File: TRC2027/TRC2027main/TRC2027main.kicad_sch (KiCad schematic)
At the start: 55 parts, among them J1 Power_conn(XT90), J10 Memory, J11 BNO055, J12 Temperature, pressure, and al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, J13 Conn_01x03_Pin, J14 Conn_01x04_Pin, J15 Conn_01x04_Pin, J16 Conn_01x04_Pin, J17 Conn_01x04_Pin, J18 Conn_01x04_Pin, J19 Conn_01x12_Pin, J2 電圧計_測定, J20 Conn_01x10_Pin, J3 電圧計_電源, J4 XH_Moter_Output, J5 XH_Moter_Output, J6 Conn_01x07_Pin, J7 GPS, J8 Conn_01x08_Pin, J9 Conn_01x08_Pin, SW1 SW_SPST, U1 DCDC, U2 DRV8262DDWR, U3 DRV8262DDWR

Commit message: change DataSheet
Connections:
- no-connect marks 43 -> 44
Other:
- moved on the sheet: A1

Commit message: add TRC2027main/SW_LED
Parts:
- removed D3: LED_RGBA, symbol Device:LED_RGBA
- added IC1: MCP23017-E_SP, KiCad_MCP23017:DIP794W56P254L3486H508Q28N, symbol MCP23017-E_SP:MCP23017-E_SP
- added J21: Conn_01x04_Pin, Connector_JST:JST_XH_B4B-XH-A_1x04_P2.50mm_Vertical, symbol Connector:Conn_01x04_Pin
- added J22, J23: XH_Moter_Output, Connector_JST:JST_XH_B2B-XH-A_1x02_P2.50mm_Vertical, symbol Connector:Conn_01x02_Pin
- added J24, J25: Conn_01x04_Pin, LED_THT:LED_D5.0mm-4_RGB, symbol Connector:Conn_01x04_Pin
- added R10: 75, Resistor_THT:R_Axial_DIN0207_L6.3mm_D2.5mm_P10.16mm_Horizontal, symbol Device:R
- added R11: 10k, Resistor_THT:R_Axial_DIN0207_L6.3mm_D2.5mm_P10.16mm_Horizontal, symbol Device:R
- added R7, R8: 10, Resistor_THT:R_Axial_DIN0207_L6.3mm_D2.5mm_P10.16mm_Horizontal, symbol Device:R
- added R9: 330, Resistor_THT:R_Axial_DIN0207_L6.3mm_D2.5mm_P10.16mm_Horizontal, symbol Device:R
- added S1: ST12-303FCG, KiCad_ST12:ST12303FCG, symbol ST12-303FCG:ST12-303FCG
- added U4, U5: DRV8262DDWR, DRV8262DDWRModule:DRV8262DDWRModule, symbol DRV8262DDWRModule:DRV8262DDWRModule
- C3: footprint (none) -> Capacitor_THT:CP_Radial_D5.0mm_P2.00mm
- C6, C8: footprint (none) -> Capacitor_SMD:C_0603_1608Metric
- C7: footprint (none) -> Capacitor_THT:CP_Radial_D8.0mm_P3.50mm
- D1, D2: footprint (none) -> LED_THT:LED_D5.0mm
- D10, D11, D12, D13, D5, D6, D7, D9: footprint UCLAMP3381PTFT -> KiCad_UCLAMP3381:UCLAMP3381PTFT
- F2: footprint 3557-15:FUSE_3557-15 -> 3557-15_fuse:FUSE_3557-15
- J1: footprint (none) -> Connector_AMASS:AMASS_XT90PW-M_1x02_P10.90mm_Horizontal
- J13: footprint (none) -> Connector_PinHeader_2.54mm:PinHeader_1x03_P2.54mm_Vertical
- J14, J15, J17, J18: footprint (none) -> Connector_JST:JST_XH_B4B-XH-A_1x04_P2.50mm_Vertical
- J16: footprint (none) -> Connector_PinHeader_2.54mm:PinHeader_1x04_P2.54mm_Vertical
- J19: footprint (none) -> Connector_PinHeader_2.54mm:PinHeader_1x12_P2.54mm_Vertical
- J2, J3, J4, J5: footprint (none) -> Connector_JST:JST_XH_B2B-XH-A_1x02_P2.50mm_Vertical
- J20: footprint (none) -> Connector_PinHeader_2.54mm:PinHeader_1x10_P2.54mm_Vertical
- J6: footprint (none) -> Connector_PinHeader_2.54mm:PinHeader_1x07_P2.54mm_Vertical
- MD1: footprint OKL-T_6-W12N-C:MURATA_OKL-T-6-W12N-C_0 -> OKL_T_6_W12N_C:MURATA_OKL-T-6-W12N-C_0
- R1, R2, R3: footprint (none) -> Resistor_THT:R_Axial_DIN0207_L6.3mm_D2.5mm_P10.16mm_Horizontal
- R4: value 330Ω -> 330; footprint (none) -> Resistor_THT:R_Axial_DIN0207_L6.3mm_D2.5mm_P10.16mm_Horizontal
- R5, R6: value 47Ω -> 10; footprint (none) -> Resistor_THT:R_Axial_DIN0207_L6.3mm_D2.5mm_P10.16mm_Horizontal
- U2, U3: footprint (none) -> DRV8262DDWRModule:DRV8262DDWRModule
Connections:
- net +24V: now also U4.3 (VM), U5.3 (VM)
- net +3.3V: now also IC1.18 (~{RESET}), IC1.9 (VDD), R10.1, S1.1, U4.9 (VCC), U5.9 (VCC)
- net +5V: now also J21.2 (Pin_2)
- net AUX: now also IC1.5 (GPB4); no longer A1.16 (GPIO12)
- net AnFAULT: now also IC1.1 (GPB0); no longer A1.17 (GPIO13)
- net BnFAULT: now also IC1.2 (GPB1); no longer A1.19 (GPIO14)
- net GND: now also IC1.10 (VSS), IC1.15 (A0), IC1.16 (A1), IC1.17 (A2), IC1.27 (GPA6), J21.1 (Pin_1), J24.2 (Pin_2), J25.2 (Pin_2), R11.1, S1.MH2, U4.4 (GND), U4.8 (GND), U5.4 (GND), U5.8 (GND)
- net PWRKEY: now also IC1.7 (GPB6); no longer A1.32 (GPIO27_ADC1)
- net RESET: now also IC1.8 (GPB7); no longer A1.31 (GPIO26_ADC0)
- net RST1: now also IC1.6 (GPB5); no longer A1.20 (GPIO15)
- net SCL: now also IC1.12 (SCL)
- net SDA: now also IC1.13 (SDA)
- net LED1: now reaches R4.2
- net LED1: now also IC1.21 (GPA0)
- net at R5.1: now also J24.3 (Pin_3)
- net LED3: now reaches R6.2
- net LED3: now also IC1.23 (GPA2)
- net GP20: no longer names the net of R4.1
- net GP20: now also J24.1 (Pin_1); no longer A1.26 (GPIO20)
- net GP21 renamed DIN2
- net DIN2: now also U5.6 (IN2); no longer R5.2
- net GP22: no longer names the net of R6.1
- net GP22: now also J24.4 (Pin_4); no longer A1.29 (GPIO22)
- net M0: no longer names the net of J6.1 (Pin_1)
- net M0: no longer A1.14 (GPIO10)
- net M1: no longer names the net of J6.2 (Pin_2)
- net M1: no longer A1.15 (GPIO11)
- new net: R11.2, S1.3
- new net: R10.2, S1.MH1
- new net: J25.1 (Pin_1), R9.1
- new net: J25.4 (Pin_4), R7.1
- new net: J25.3 (Pin_3), R8.1
- new net CIN1: A1.14 (GPIO10), U4.7 (IN1)
- new net CIN2: A1.15 (GPIO11), U4.6 (IN2)
- new net COUT1: J23.1 (Pin_1), U4.1 (OUT1)
- new net COUT2: J23.2 (Pin_2), U4.2 (OUT2)
- new net CnFAULT: IC1.3 (GPB2), U4.5 (nFAULT)
- new net DIN1: A1.26 (GPIO20), U5.7 (IN1)
- new net DOUT1: J22.1 (Pin_1), U5.1 (OUT1)
- new net DOUT2: J22.2 (Pin_2), U5.2 (OUT2)
- new net DnFAULT: IC1.4 (GPB3), U5.5 (nFAULT)
- new net LED2: IC1.22 (GPA1), R5.2
- new net LED4: IC1.24 (GPA3), R9.2
- new net LED5: IC1.25 (GPA4), R8.2
- new net LED6: IC1.26 (GPA5), R7.2
- no-connect marks 44 -> 53
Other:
- moved on the sheet: A1, C3, D12, D13, D5, D6, J16, J4, J5

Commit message: new file:   TRC2027/R_Sokutei/R_Sokutei-backups/R_Sokutei-2026-04-18_181141.zip
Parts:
- added C10, C11, C9: 100u, Capacitor_THT:CP_Radial_D8.0mm_P3.50mm, symbol Device:C_Polarized
- added D3, D4: UCLAMP3381P.TFT, KiCad_UCLAMP3381:UCLAMP3381PTFT, symbol UCLAMP3381P_TFT:UCLAMP3381P.TFT
- added J26, J27, J28: Conn_01x03_Pin, Connector_JST:JST_XH_B3B-XH-A_1x03_P2.50mm_Vertical, symbol Connector:Conn_01x03_Pin
- J24, J25: footprint LED_THT:LED_D5.0mm-4_RGB -> Connector_JST:JST_XH_B4B-XH-A_1x04_P2.50mm_Vertical
- MD1: footprint OKL_T_6_W12N_C:MURATA_OKL-T-6-W12N-C_0 -> OKL_T_6_W12N_C:OKL-T&slash_6-W12N-C-Kai
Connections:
- net +5V: now also C10.1, C11.1, C9.1, J26.2 (Pin_2), J27.2 (Pin_2), J28.2 (Pin_2)
- net GND: now also C10.2, C11.2, C9.2, D3.2, D4.2, J26.1 (Pin_1), J27.1 (Pin_1), J28.1 (Pin_1); no longer IC1.27 (GPA6)
- net RX2: now also J21.4 (Pin_4), D3.1
- net TX2: now also J21.3 (Pin_3), D4.1
- net LEDSW: now reaches R11.2, S1.3
- net LEDSW: now also IC1.27 (GPA6)
- net PWM: now reaches A1.16 (GPIO12)
- net PWM: now also J26.3 (Pin_3)
- net PWM2: now reaches A1.17 (GPIO13)
- net PWM2: now also J27.3 (Pin_3)
- net PWM3: now reaches A1.19 (GPIO14)
- net PWM3: now also J28.3 (Pin_3)
- no-connect marks 53 -> 51
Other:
- moved on the sheet: R11

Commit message: add
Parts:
- removed A1: RaspberryPi_Pico, Module:RaspberryPi_Pico_Common_Unspecified, symbol MCU_Module:RaspberryPi_Pico
- removed C10: 100u, Capacitor_THT:CP_Radial_D8.0mm_P3.50mm, symbol Device:C_Polarized
- removed C3: 47u, Capacitor_THT:CP_Radial_D5.0mm_P2.00mm, symbol Device:C_Polarized
- removed D10, D11, D12, D13, D3, D4, D5, D6, D7, D9: UCLAMP3381P.TFT, KiCad_UCLAMP3381:UCLAMP3381PTFT, symbol UCLAMP3381P_TFT:UCLAMP3381P.TFT
- removed IC1: MCP23017-E_SP, KiCad_MCP23017:DIP794W56P254L3486H508Q28N, symbol MCP23017-E_SP:MCP23017-E_SP
- removed J10: Memory, Connector_PinSocket_2.54mm:PinSocket_1x07_P2.54mm_Vertical, symbol Connector:Conn_01x07_Pin
- removed J11: BNO055, Connector_PinSocket_2.54mm:PinSocket_1x04_P2.54mm_Vertical, symbol Connector:Conn_01x04_Pin
- removed J12: Temperature, pressure, and altitude sensor, Connector_PinSocket_2.54mm:PinSocket_1x07_P2.54mm_Vertical, symbol Connector:Conn_01x07_Pin
- removed J13: Conn_01x03_Pin, Connector_PinHeader_2.54mm:PinHeader_1x03_P2.54mm_Vertical, symbol Connector:Conn_01x03_Pin
- removed J14, J15, J17, J18, J21, J24, J25: Conn_01x04_Pin, Connector_JST:JST_XH_B4B-XH-A_1x04_P2.50mm_Vertical, symbol Connector:Conn_01x04_Pin
- removed J16: Conn_01x04_Pin, Connector_PinHeader_2.54mm:PinHeader_1x04_P2.54mm_Vertical, symbol Connector:Conn_01x04_Pin
- removed J19: Conn_01x12_Pin, Connector_PinHeader_2.54mm:PinHeader_1x12_P2.54mm_Vertical, symbol Connector:Conn_01x12_Pin
- removed J20: Conn_01x10_Pin, Connector_PinHeader_2.54mm:PinHeader_1x10_P2.54mm_Vertical, symbol Connector:Conn_01x10_Pin
- removed J6: Conn_01x07_Pin, Connector_PinHeader_2.54mm:PinHeader_1x07_P2.54mm_Vertical, symbol Connector:Conn_01x07_Pin
- removed J7: GPS, Connector_PinSocket_2.54mm:PinSocket_1x04_P2.54mm_Vertical, symbol Connector:Conn_01x04_Pin
- removed J8, J9: Conn_01x08_Pin, Connector_PinHeader_2.54mm:PinHeader_1x08_P2.54mm_Vertical, symbol Connector:Conn_01x08_Pin
- removed R10: 75, Resistor_THT:R_Axial_DIN0207_L6.3mm_D2.5mm_P10.16mm_Horizontal, symbol Device:R
- removed R11: 10k, Resistor_THT:R_Axial_DIN0207_L6.3mm_D2.5mm_P10.16mm_Horizontal, symbol Device:R
- removed R4, R9: 330, Resistor_THT:R_Axial_DIN0207_L6.3mm_D2.5mm_P10.16mm_Horizontal, symbol Device:R
- removed R5, R6, R7, R8: 10, Resistor_THT:R_Axial_DIN0207_L6.3mm_D2.5mm_P10.16mm_Horizontal, symbol Device:R
- removed S1: ST12-303FCG, KiCad_ST12:ST12303FCG, symbol ST12-303FCG:ST12-303FCG
- added J30: Conn_01x20_Pin, Connector_JST:JST_XH_B20B-XH-A_1x20_P2.50mm_Vertical, symbol Connector:Conn_01x20_Pin
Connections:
- net +3.3V: now also J30.4 (Pin_4)
- net +5V: now also J30.5 (Pin_5)
- net AIN1: now also J30.20 (Pin_20)
- net AIN2: now also J30.19 (Pin_19)
- net AnFAULT: now also J30.9 (Pin_9)
- net BIN1: now also J30.18 (Pin_18)
- net BIN2: now also J30.17 (Pin_17)
- net BnFAULT: now also J30.8 (Pin_8)
- net CIN1: now also J30.16 (Pin_16)
- net CIN2: now also J30.15 (Pin_15)
- net CnFAULT: now also J30.7 (Pin_7)
- net DIN1: now also J30.14 (Pin_14)
- net DIN2: now also J30.13 (Pin_13)
- net DnFAULT: now also J30.6 (Pin_6)
- net GND: now also J30.3 (Pin_3)
- net PWM: now also J30.12 (Pin_12)
- net PWM2: now also J30.11 (Pin_11)
- net PWM3: now also J30.10 (Pin_10)
- no-connect marks 51 -> 11
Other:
- moved on the sheet: C11, C9, J26, J27, J28

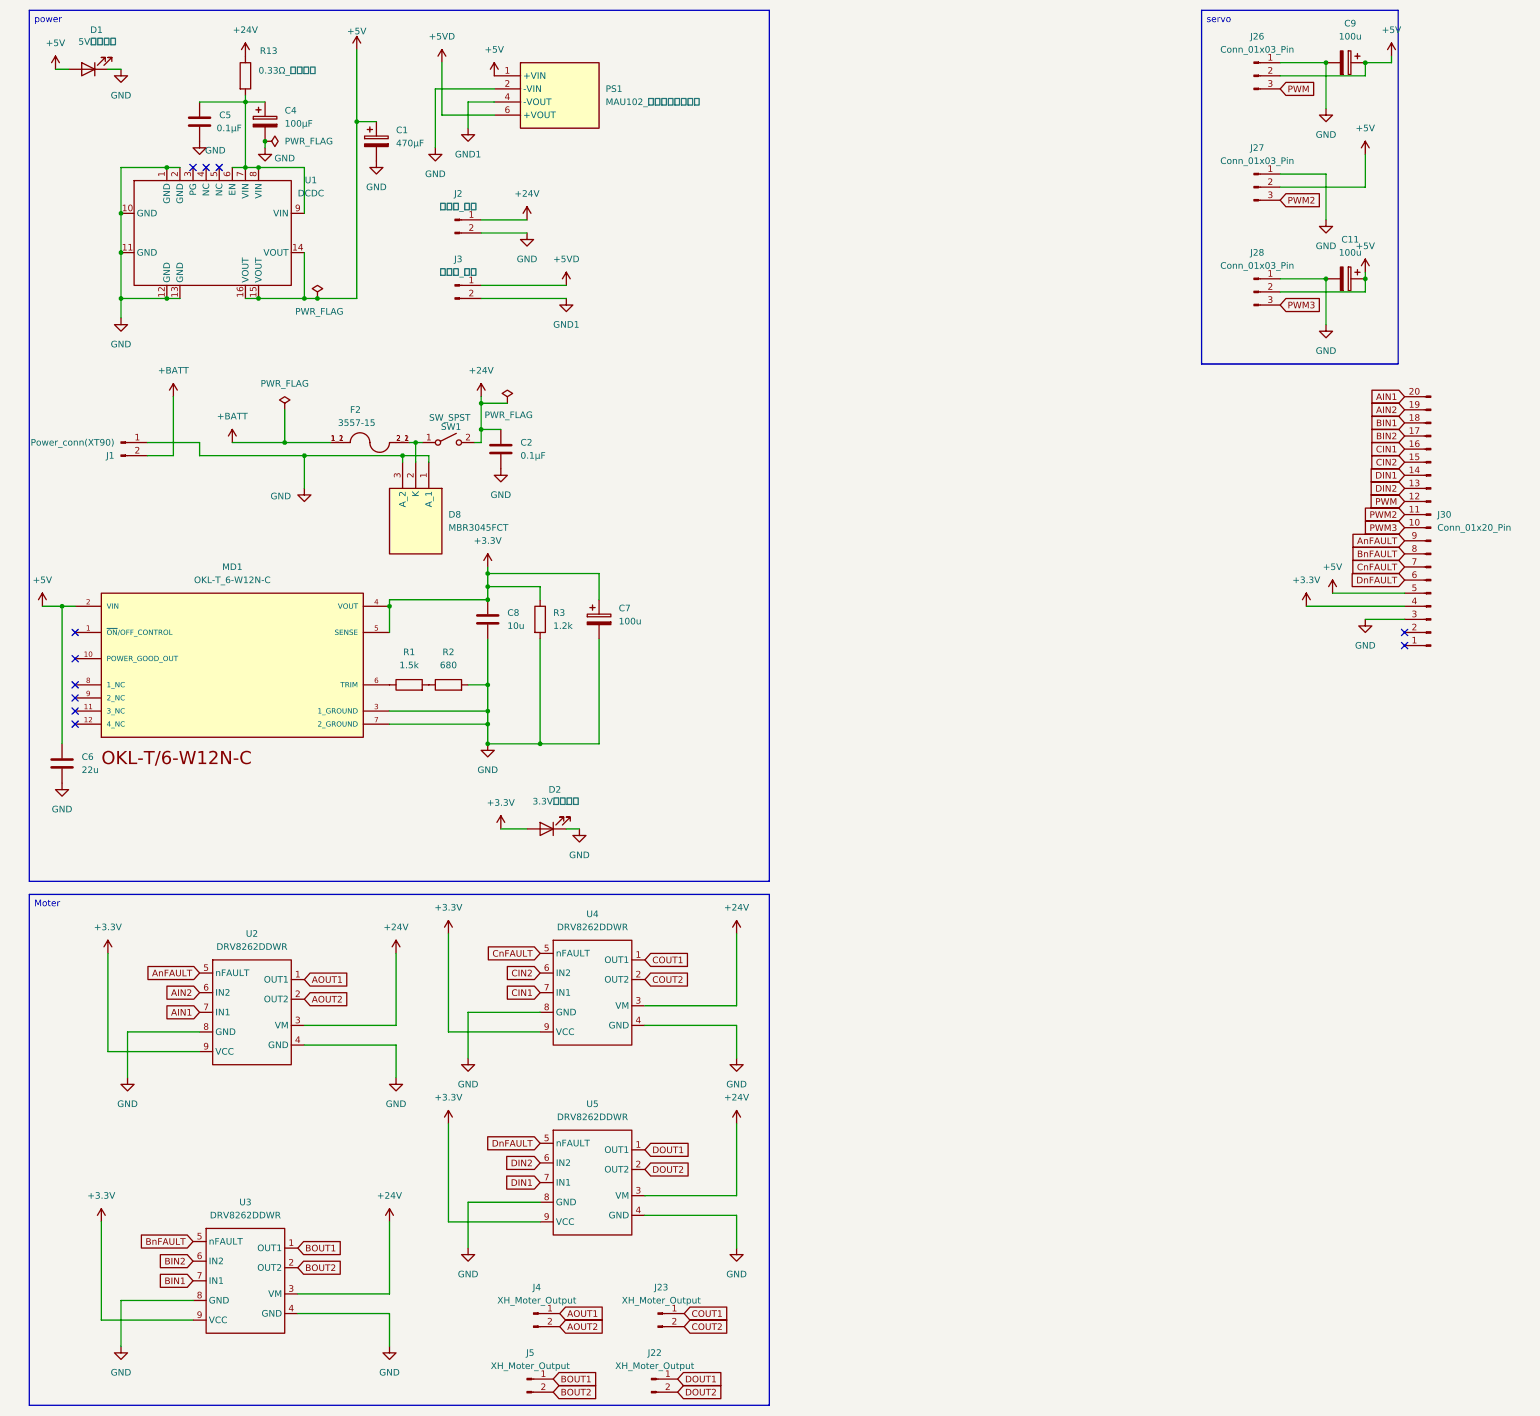
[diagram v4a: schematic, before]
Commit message: Add positions.csv file with component placements and orientations
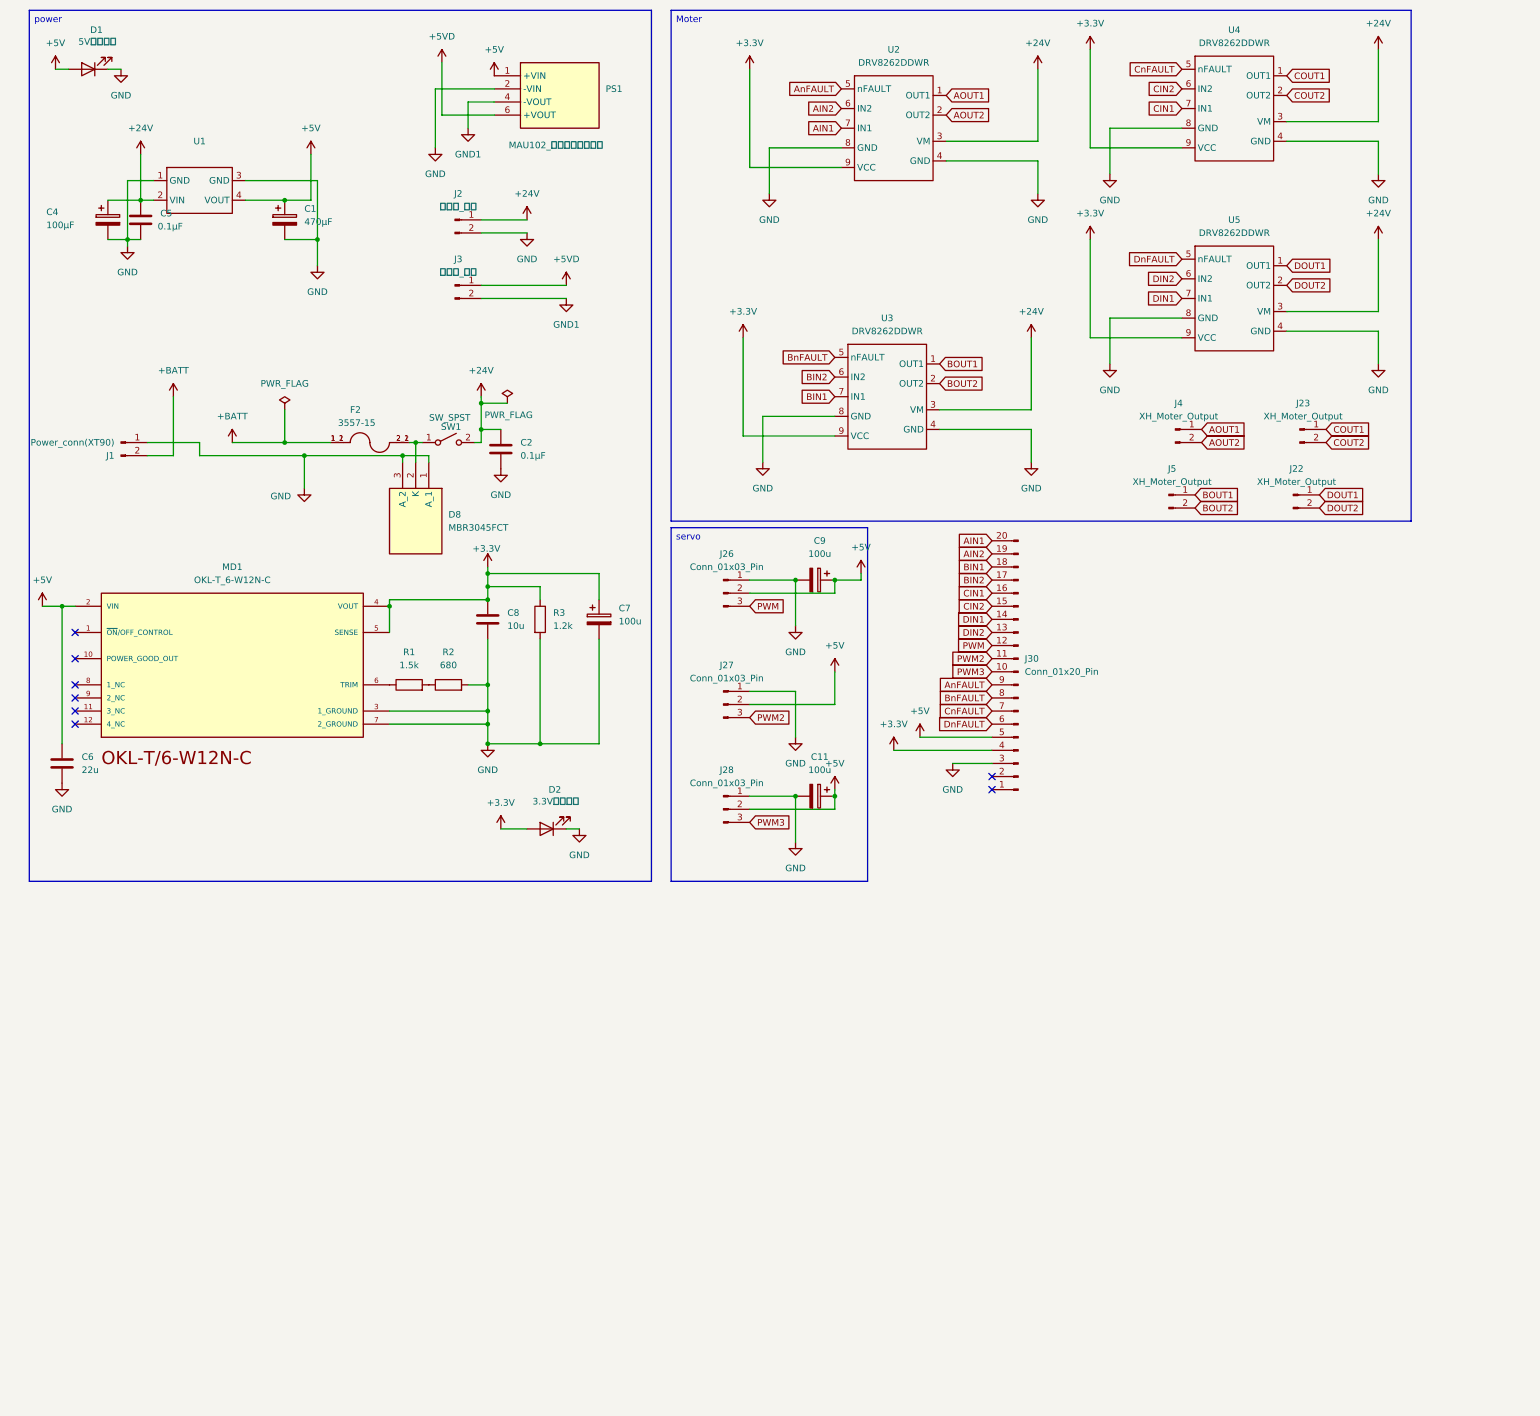
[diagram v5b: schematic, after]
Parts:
- removed R13: 0.33Ω_金属皮膜, Resistor_THT:R_Axial_DIN0516_L15.5mm_D5.0mm_P20.32mm_Horizontal, symbol Device:R
- removed U1: DCDC, LMR38025:LMR, symbol LMR38025-Strawberry:LMR38025-Strawberry
- added U1: ~, LM70880Module:LM70880Module, symbol LM70880Module:LM70880Module
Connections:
- net +24V: now also C4.1, C5.1, U1.2 (VIN)
- net +5V: now also U1.4 (VOUT)
- net GND: now also U1.1 (GND), U1.3 (GND)
- no-connect marks 11 -> 8
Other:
- moved on the sheet: C1, C11, C4, C5, C9, J22, J23, J26, J27, J28, J30, J4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
